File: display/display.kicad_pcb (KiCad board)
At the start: 2 copper layers, 52 x 52 mm, 37 parts, among them J1 Conn_01x02, J2 Conn_01x03, J3 Conn_01x05, U1 74HC238, U2 74HC238

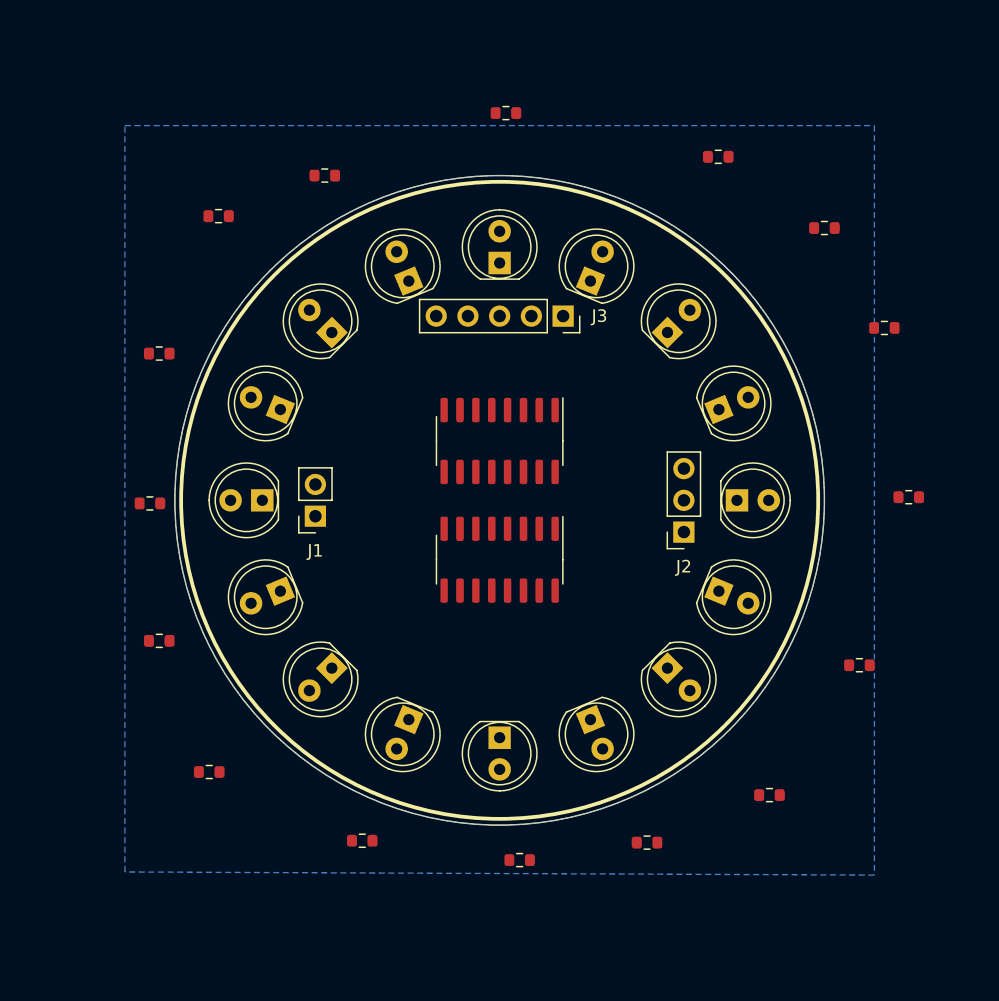
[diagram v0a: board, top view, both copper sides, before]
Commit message: resize boards
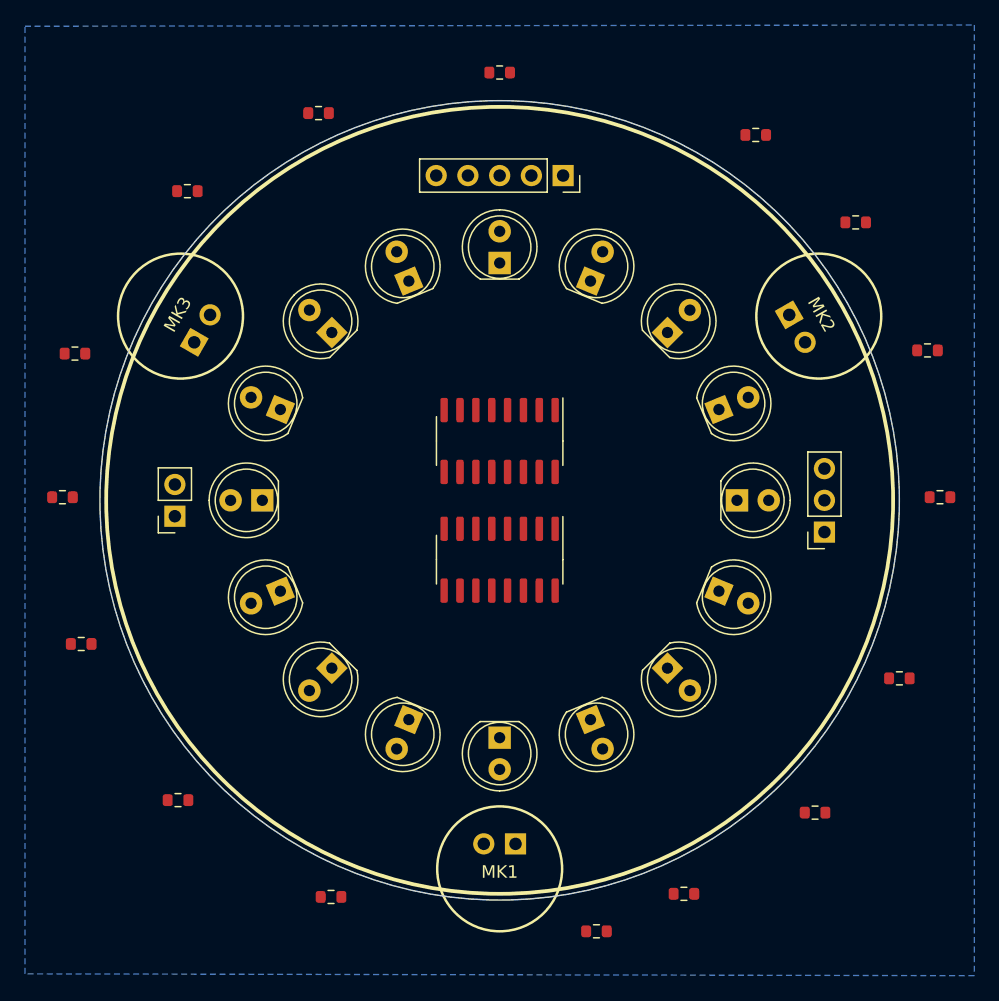
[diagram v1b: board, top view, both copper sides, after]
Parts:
- added MK1: Microphone, df-parts:CMA-6542PF, F.Cu at (150.3, 126.0)
- added MK2: Microphone, df-parts:CMA-6542PF, F.Cu at (175.9, 81.8)
- added MK3: Microphone, df-parts:CMA-6542PF, F.Cu at (124.8, 81.8)
- moved J1 11.2 mm to (124.3, 97.8)
- moved J2 11.2 mm to (176.3, 99.1)
- moved J3 11.2 mm to (155.4, 70.5)
- moved R9 8.39 mm to (158.1, 131.1)
- moved R13 7.02 mm to (115.3, 96.3)
- moved R14 6.75 mm to (116.3, 84.8)
- moved R12 6.25 mm to (116.8, 108.0)
- moved R10 5.15 mm to (136.8, 128.3)
- moved R8 5.05 mm to (165.1, 128.1)
- moved R16 5.02 mm to (135.8, 65.5)
- moved R7 3.91 mm to (175.6, 121.5)
- moved R4 3.89 mm to (184.6, 84.5)
- moved R2 3.47 mm to (170.8, 67.3)
- moved R6 3.37 mm to (182.3, 110.8)
- moved R11 3.36 mm to (124.6, 120.5)
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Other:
- board size 52 x 52 mm -> 64 x 64 mm

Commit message: display pcb wired
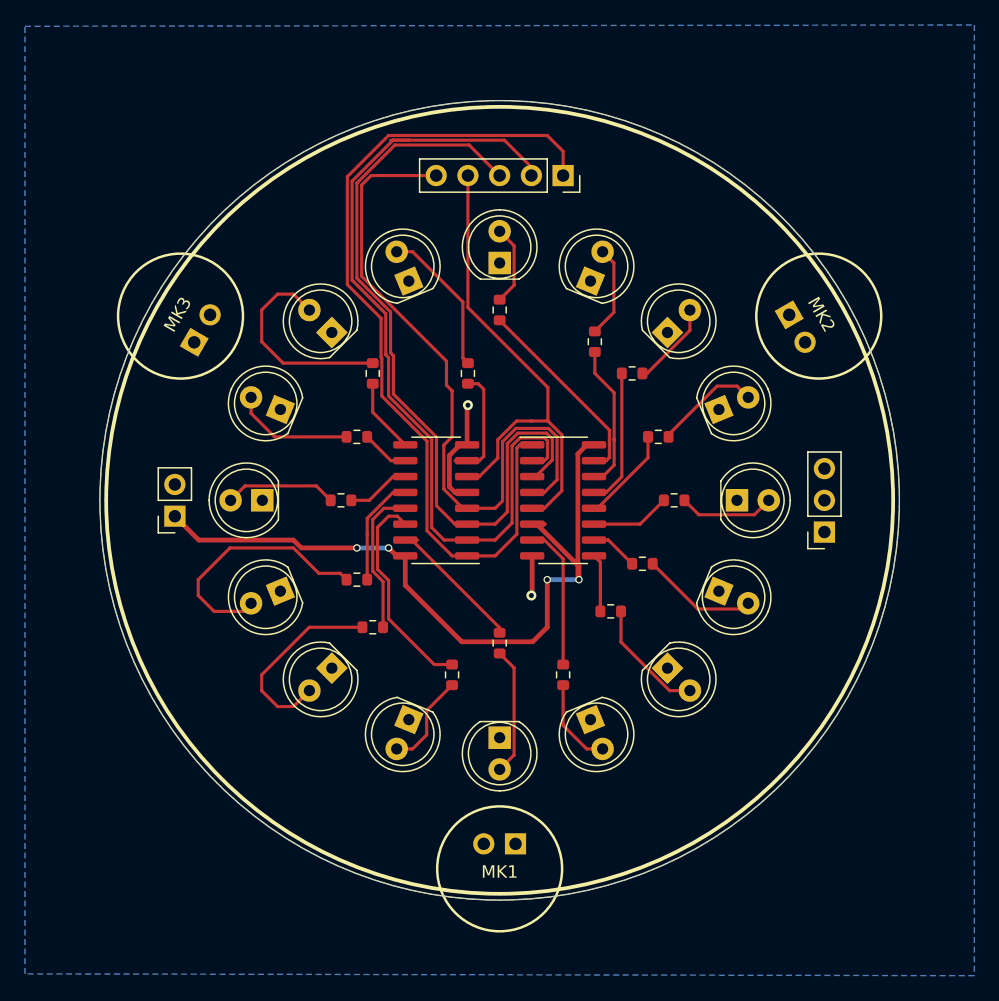
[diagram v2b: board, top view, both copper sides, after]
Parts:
- moved R9 24.3 mm to (150.3, 108.0), turned to 90 degrees
- moved R16 24.0 mm to (147.8, 86.4), turned to 270 degrees
- moved R14 23.5 mm to (138.9, 91.5)
- moved R7 23.0 mm to (159.2, 105.4), turned to 180 degrees
- moved R12 22.7 mm to (138.9, 102.9)
- moved R4 22.6 mm to (163.1, 91.5), turned to 180 degrees
- moved R6 22.5 mm to (161.8, 101.6), turned to 180 degrees
- moved R13 22.3 mm to (137.7, 96.5)
- moved R3 21.6 mm to (161.0, 86.4), turned to 180 degrees
- moved R5 21.3 mm to (164.3, 96.5), turned to 180 degrees
- moved R2 21.0 mm to (158.0, 83.8), turned to 270 degrees
- moved R11 20.8 mm to (140.2, 106.7)
- moved R15 20.8 mm to (140.2, 86.4), turned to 270 degrees
- moved R10 20.2 mm to (146.5, 110.5), turned to 90 degrees
- moved R8 20.0 mm to (155.4, 110.5), turned to 90 degrees
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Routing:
- net D0: track 0.00 -> 69.1 mm
- net D1: track 0.00 -> 68.6 mm
- net D2: track 0.00 -> 62.3 mm
- net +5V: track 0.00 -> 61.7 mm, vias 0 -> 4
- net GlobalEn: track 0.00 -> 55.1 mm
- net D3: track 0.00 -> 40.5 mm
- net Net-(D12-Pad2): track 0.00 -> 20.3 mm
- net Net-(R10-Pad2): track 0.00 -> 17.4 mm
- net Net-(D15-Pad2): track 0.00 -> 17.0 mm
- net Net-(R1-Pad2): track 0.00 -> 16.0 mm
- net Net-(D11-Pad2): track 0.00 -> 15.8 mm
- net GND: track 0.00 -> 13.6 mm, vias 0 -> 2
- net Net-(R11-Pad2): track 0.00 -> 12.9 mm
- net Net-(D16-Pad2): track 0.00 -> 12.7 mm
- net Net-(R9-Pad2): track 0.00 -> 11.8 mm
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
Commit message: errata 2: fix footprints
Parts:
- J1: footprint Connector_PinSocket_2.54mm:PinSocket_1x02_P2.54mm_Vertical -> df-parts:310-XX-102-41-001000
- J2: footprint Connector_PinSocket_2.54mm:PinSocket_1x03_P2.54mm_Vertical -> df-parts:310-XX-103-41-001000
- J3: footprint Connector_PinSocket_2.54mm:PinSocket_1x05_P2.54mm_Vertical -> df-parts:310-XX-105-41-001000
